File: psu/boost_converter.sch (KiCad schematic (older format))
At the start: 90 parts, among them IC10 AD8551, IC11 AD8551, IC12 AD8551, IC5 NCV8460A, IC6 MCP1416, IC7 MCP1416, IC8 MCP1416, IC9 INA139, Q1 STB45N60DM2AG, Q2 STB45N60DM2AG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

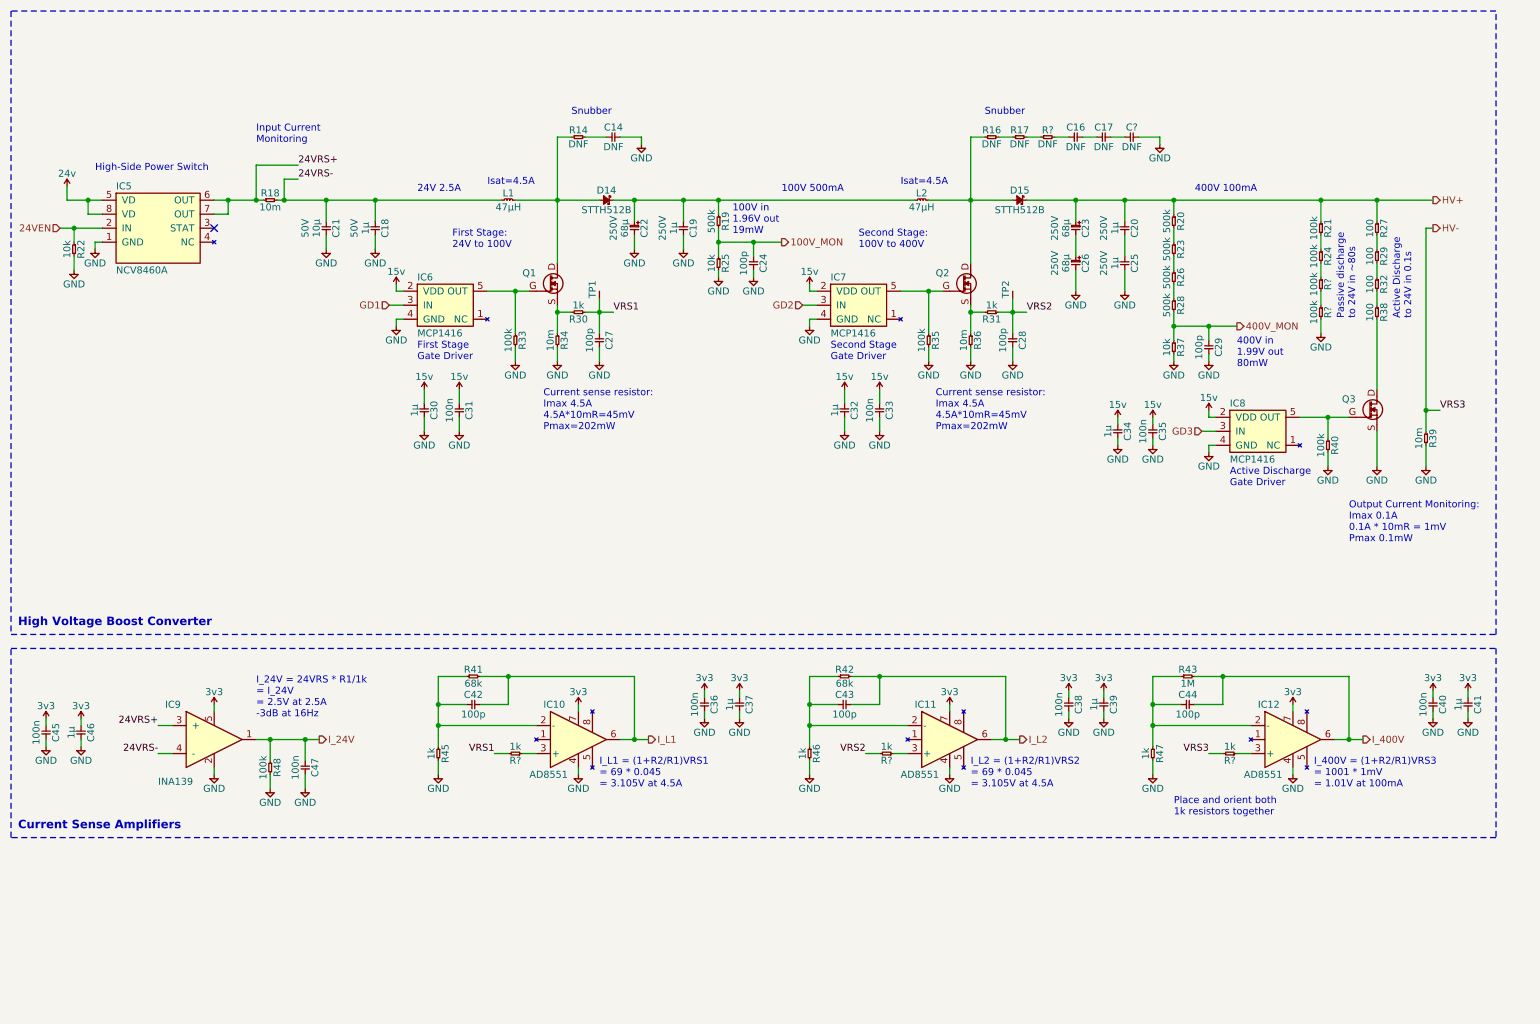
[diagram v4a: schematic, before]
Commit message: update before swapping to flyback
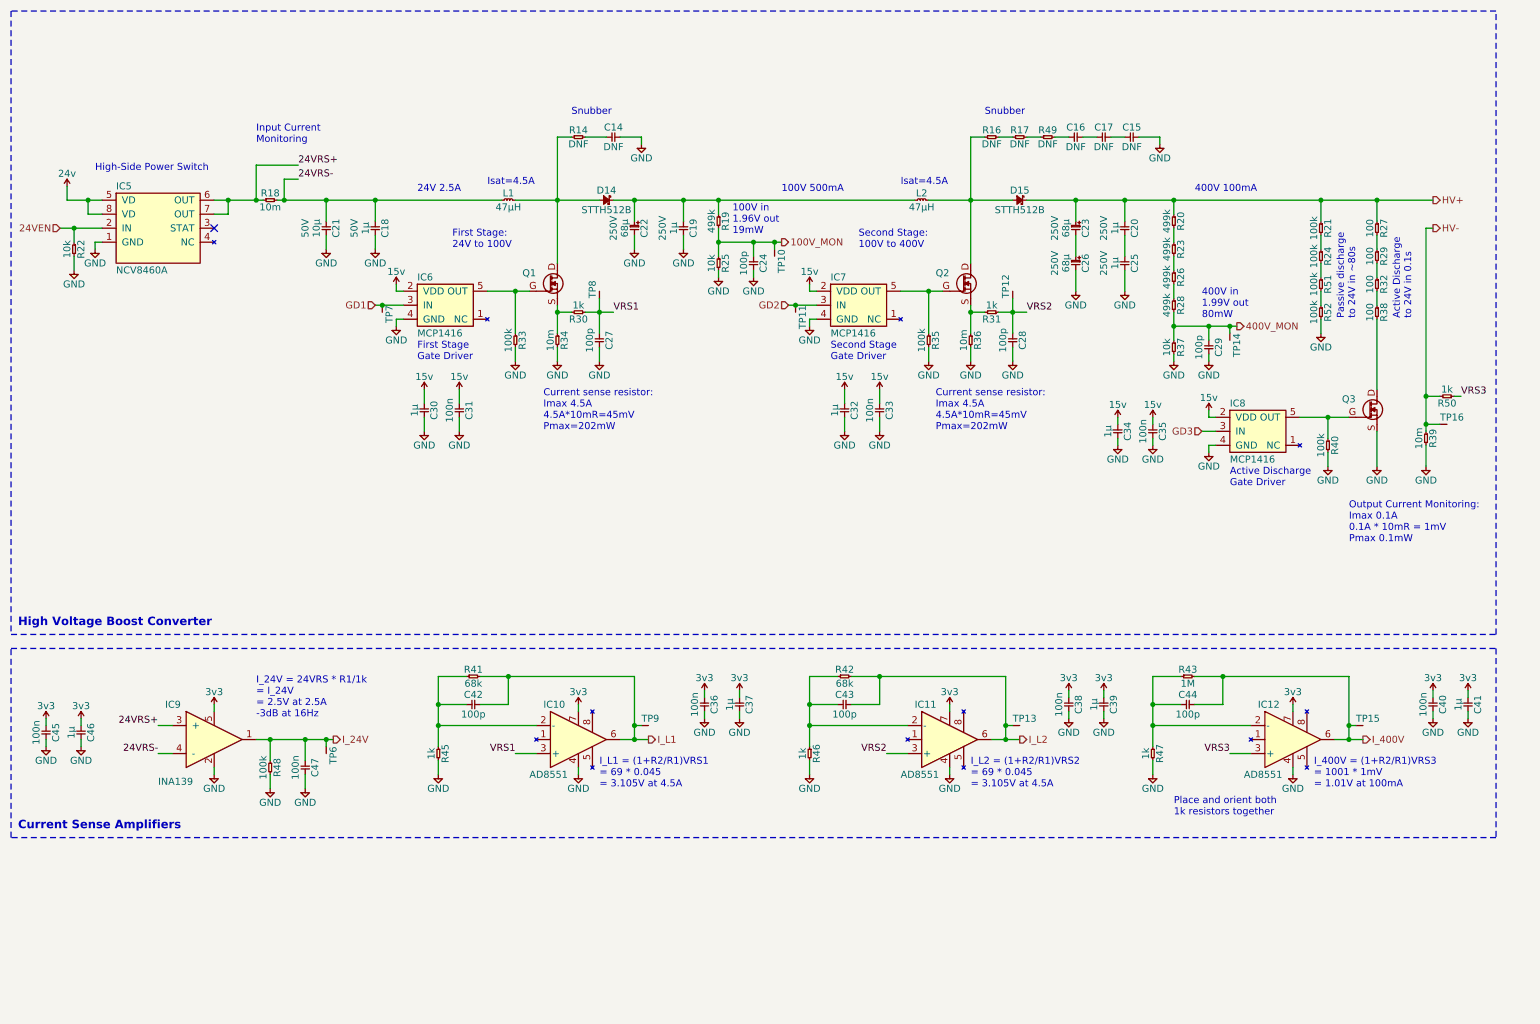
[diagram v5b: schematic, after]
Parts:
- removed R? (x2): 1k, agg:0603, symbol agg:R
- added TP10, TP13, TP14, TP15, TP16, TP6, TP9: TESTPAD, agg:TESTPAD, symbol agg:TESTPAD
- added TP11, TP7: TESTPAD, agg:SIL-254P-01, symbol agg:TESTPAD
- C14, C16: Voltage 250 -> 250V
- C21: footprint (none) -> agg:1210; Farnell (none) -> 2781426
- C22, C23, C26: footprint (none) -> agg:PANASONIC-SMDCAP-K
- C24, C27, C28, C29: Farnell (none) -> 9406115; Voltage 50 -> 50V
- C30, C32, C34: footprint agg:0805 -> agg:1206; Farnell (none) -> 1759454; Voltage 50 -> 50V
- C31, C33, C35, C36, C38, C40, C45, C47: Farnell (none) -> 2320803; Voltage 50 -> 50V
- C37, C39, C41, C46: Farnell (none) -> 2320814; Voltage 16 -> 16V
- C42, C43, C44: Farnell (none) -> 9406115; Voltage (none) -> 50V
- R18, R34, R36, R39: footprint agg:1210 -> agg:1206; Farnell (none) -> 2079442
- R19, R20, R23, R26, R28: value 500k -> 499k; Farnell (none) -> 2447667; Voltage (none) -> 150V
- R21, R24: footprint agg:0805 -> agg:1206; Farnell (none) -> 2447453; Voltage (none) -> 200V
- R22: Farnell (none) -> 2447230; Voltage (none) -> 50V
- R25, R37: footprint agg:0805 -> agg:0603; Farnell (none) -> 2447230; Voltage (none) -> 50V
- R27, R29, R32, R38: footprint agg:1210 -> agg:D2PAK_R; Farnell (none) -> 2101651
- R30, R31: footprint agg:0805 -> agg:0603; Farnell (none) -> 2447272; Voltage (none) -> 50V
- R33, R35, R40, R48: Farnell (none) -> 2447226; Voltage (none) -> 50V
- R41, R42: Farnell (none) -> 2447420; Voltage (none) -> 50V
- R43: Farnell (none) -> 2447285; Voltage (none) -> 50V
- R45, R46, R47: Farnell (none) -> 2447272; Voltage (none) -> 50V
- R50: renamed from R?; Farnell (none) -> 2447272; Voltage (none) -> 50V
- R51, R52: renamed from R?; footprint agg:0805 -> agg:1206; Farnell (none) -> 2447453; Voltage (none) -> 200V
- gave numbers to parts that had none: 2
- renumbered TP2 to TP12, TP1 to TP8
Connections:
- net 100V_MON: now also TP10.1 (TP)
- net 400V_MON: now also TP14.1 (TP)
- net GD1: now also TP7.1 (TP)
- net GD2: now also TP11.1 (TP)
- net HV-: now also TP16.1 (TP)
- net I_24V: now also TP6.1 (TP)
- net I_400V: now also TP15.1 (TP)
- net I_L1: now also TP9.1 (TP)
- net I_L2: now also TP13.1 (TP)
- net VRS1: now also IC10.3 (+)
- net VRS2: now also IC11.3 (+)
- net VRS3: now reaches IC12.3 (+), R50.1
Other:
- moved on the sheet: R50
